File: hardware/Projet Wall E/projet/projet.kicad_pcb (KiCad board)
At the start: 4 copper layers, 110 parts, among them J201 USB_C_Receptacle_USB2.0_16P, J202 Conn_01x02, J301 Conn_ST_STDC14, J302 Conn_01x03, J401 Conn_01x06, J402 Conn_01x06, J501 Conn_01x06, J502 Conn_01x06, J503 Conn_01x03, J504 Conn_01x06, Q201 2SK3019, Q202 MMDT5401, Q203 DMP3099L, U201 AP2112K-3.3, U202 BQ27220YZFR, U203 USBLC6-2SC6, U204 BQ25896RTW, U301 STM32G431RBTx, U401 DRV8833PWP, U501 SN74AHCT1G125DBVR, Y301 16MHz

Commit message: PCB : placement final avant routage
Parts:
- removed TP210, TP211: GND, TestPoint:TestPoint_Pad_D1.5mm
- moved H302 163.7 mm to (200.5, 57.1)
- moved H304 161.1 mm to (200.5, 90.5)
- moved R203 155.8 mm to (197.1, 73.4), turned to 180 degrees
- moved R202 154.2 mm to (196.3, 60.7), turned to 180 degrees
- moved J201 144.5 mm to (199.5, 67.0), turned to 90 degrees
- moved Q202 142.9 mm to (181.5, 62.3)
- moved R211 138.6 mm to (183.7, 61.0), turned to 90 degrees
- moved J302 137.4 mm to (186.2, 56.1), turned to 90 degrees
- moved R208 134.5 mm to (179.3, 62.8), turned to -90 degrees
- moved C313 132.7 mm to (190.2, 58.6)
- moved U203 127.3 mm to (190.7, 67.2), turned to 180 degrees
- moved Q203 123.3 mm to (181.5, 65.7), turned to -90 degrees
- moved J301 121.4 mm to (164.2, 65.5), turned to 180 degrees
- moved C404 113.5 mm to (188.9, 78.6)
- moved J402 112.2 mm to (179.7, 88.7)
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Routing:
- net GND: track 0.00 -> 1.52 mm
- net /Moteur/AOUT2: track 0.00 -> 1.27 mm, vias 0 -> 1
- net /Moteur/BOUT2: track 0.00 -> 1.27 mm, vias 0 -> 1
- added copper zone on In1.Cu, net GND

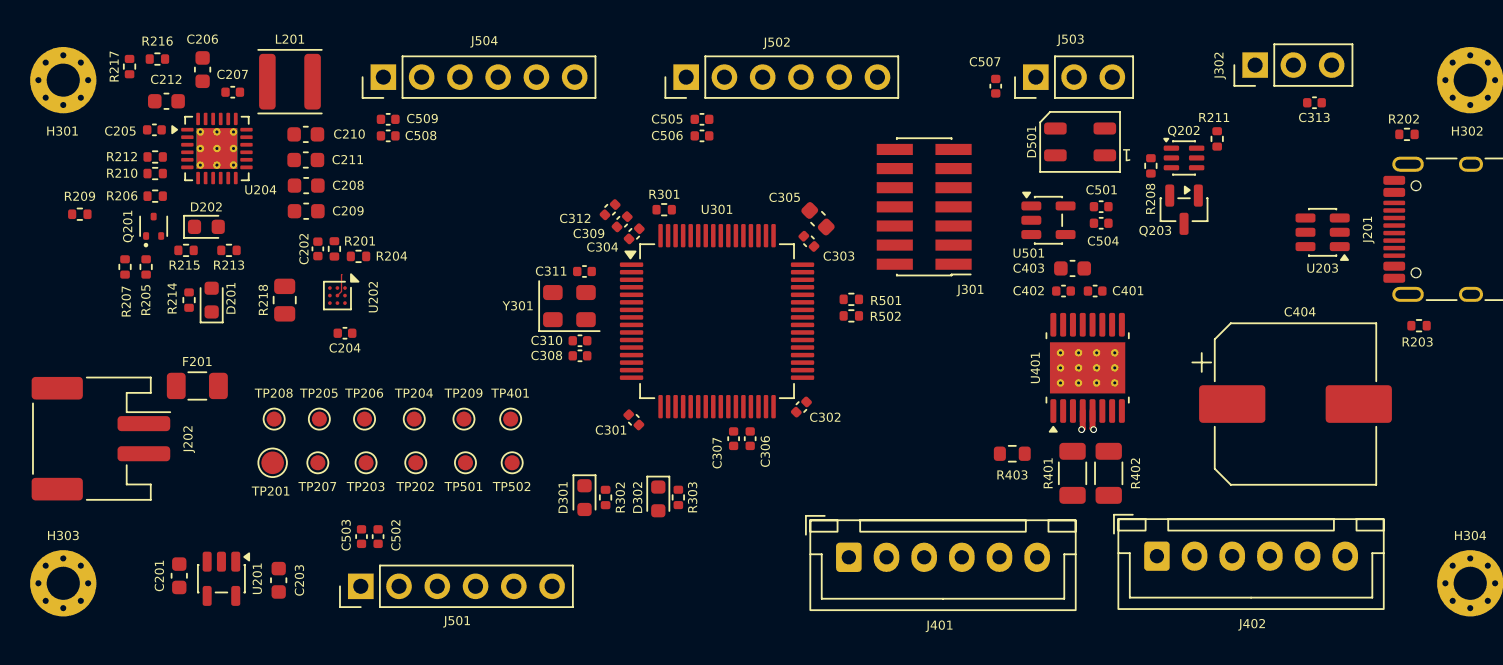
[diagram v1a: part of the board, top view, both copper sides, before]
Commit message: PCB : routage GND et alimentations
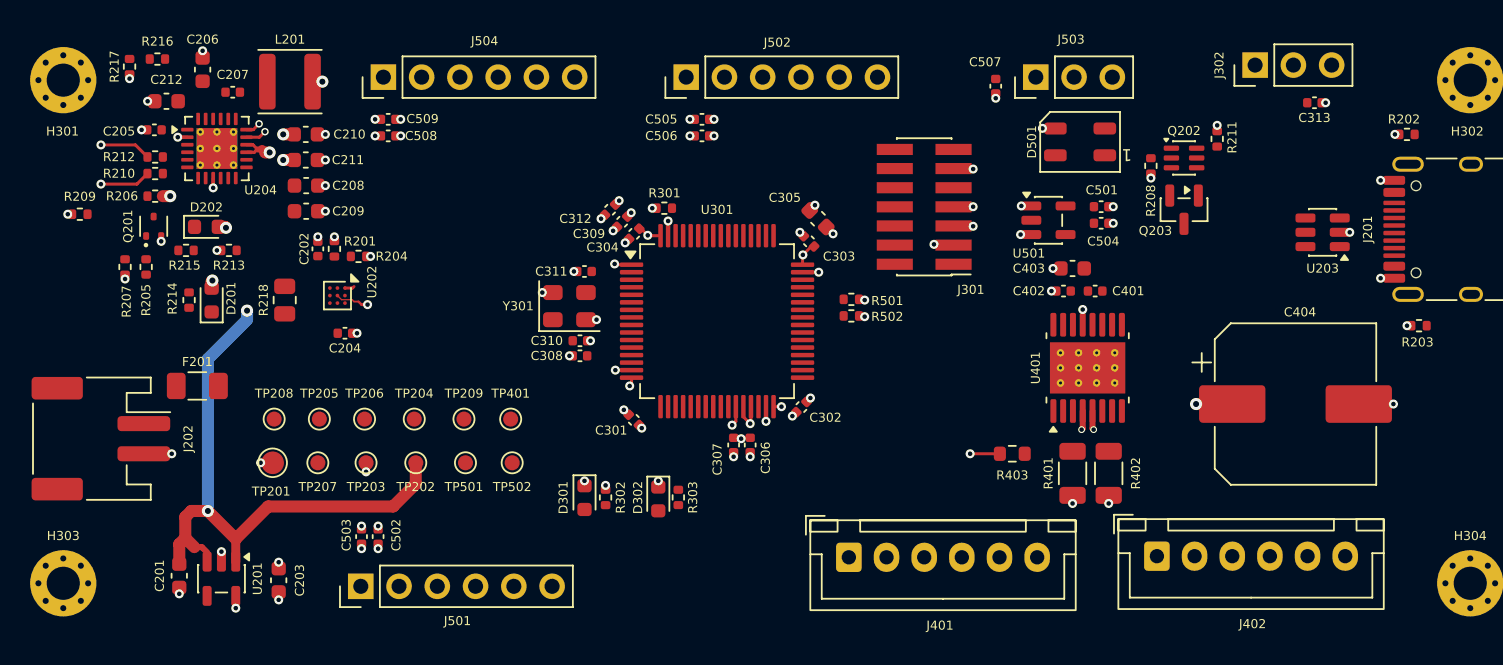
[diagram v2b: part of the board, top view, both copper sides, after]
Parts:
- moved C306 0.42 mm to (152.7, 81.3)
- moved C307 0.42 mm to (151.6, 81.3)
- moved R301 0.10 mm to (147.0, 65.6)
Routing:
- net VSYS: track 0.00 -> 47.0 mm, vias 0 -> 9
- net GND: track 1.52 -> 45.6 mm, vias 0 -> 75
- net +3.3V: track 0.00 -> 27.1 mm, vias 0 -> 30
- net +5V_USB: track 0.00 -> 2.40 mm, vias 0 -> 1
- net /Alimentation/GAUGE_INT: track 0.00 -> 0.64 mm
- added copper zone on In2.Cu, net +3.3V
- added copper zone on In2.Cu, net +5V_USB
- added copper zone on In2.Cu, net VSYS
